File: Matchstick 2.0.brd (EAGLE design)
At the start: 73 x 38 mm, 13 parts, among them IC1 74HCT125D, J1 694106301002, J2 TARGET, J3 691241510006, J4 691241510006, U1 M5STAMP PICO

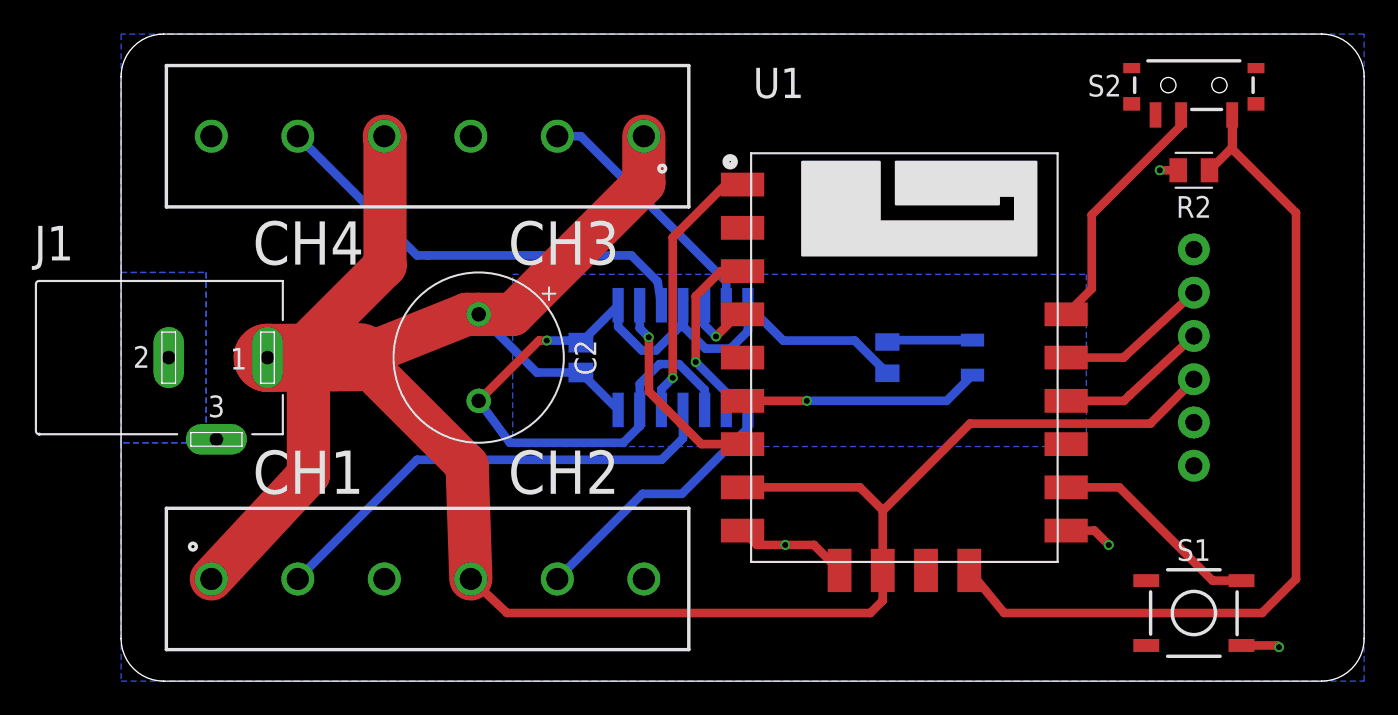
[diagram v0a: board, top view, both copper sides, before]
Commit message: adjusting traces for solderability
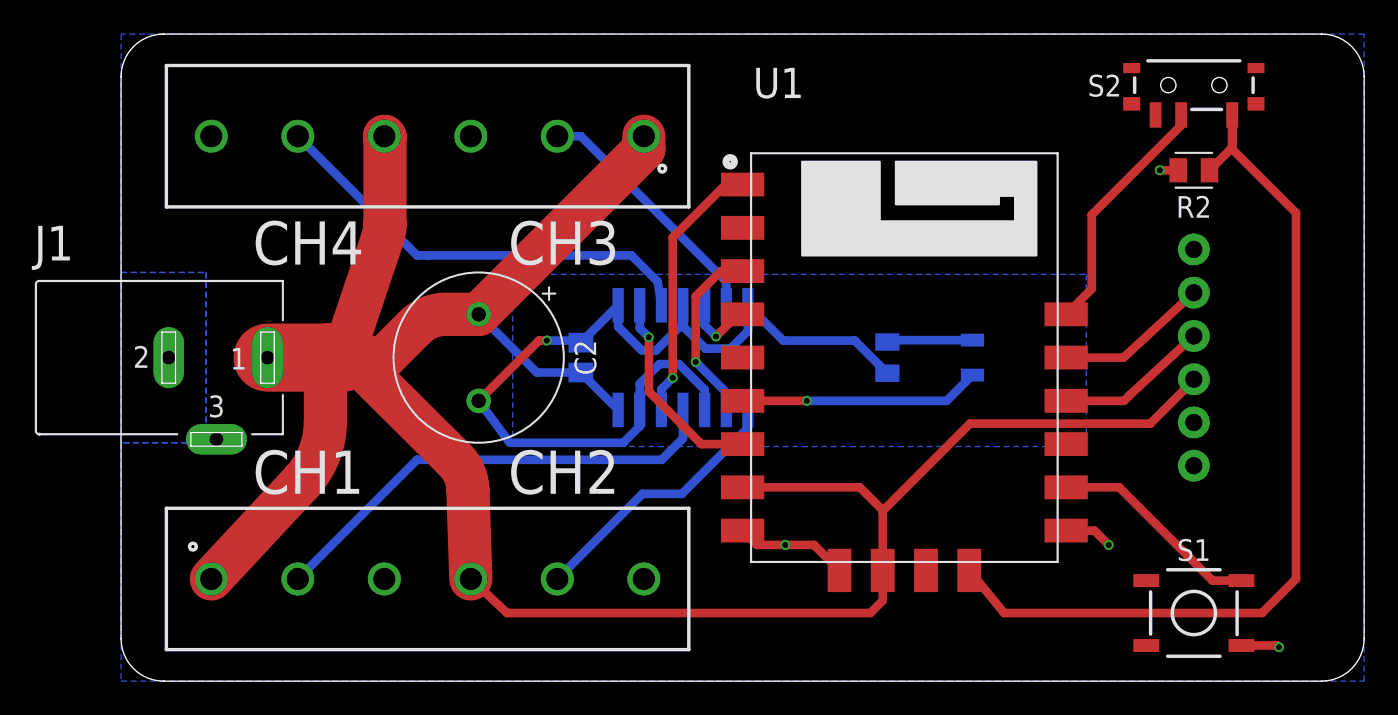
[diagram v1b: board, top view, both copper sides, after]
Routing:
- net VCC: track 155.1 -> 145.6 mm
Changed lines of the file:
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@@
 <wire x1="63" y1="17.73" x2="62.98" y2="17.65605" width="0.508" layer="1"/>
 <wire x1="62.98" y1="17.65605" x2="60.44755" y2="15.1236" width="0.508" layer="1"/>
-<wire x1="20.54" y1="6" x2="20.32" y2="12.68" width="2.54" layer="1"/>
+<wire x1="20.54" y1="6" x2="20.36624375" y2="11.2758625" width="2.54" layer="1"/>
+<wire x1="20.36624375" y1="11.2758625" x2="19.6312375" y2="12.96549375" width="2.54" layer="1" curve="43.247949"/>
+<wire x1="19.6312375" y1="12.96549375" x2="13.56851875" y2="19" width="2.54" layer="1"/>
 <wire x1="20.54" y1="6" x2="22.67" y2="4" width="0.508" layer="1"/>
 <wire x1="15.46" y1="32" x2="15.5" y2="31.96" width="2.54" layer="1"/>
-<wire x1="15.5" y1="31.96" x2="15.5" y2="24.4" width="2.54" layer="1"/>
-<wire x1="5.3" y1="6" x2="11" y2="12.121946875" width="2.54" layer="1"/>
-<wire x1="15.5" y1="24.4" x2="10.13125" y2="19.03125" width="2.54" layer="1"/>
-<wire x1="10.13125" y1="19.03125" x2="8.6" y2="19" width="2.54" layer="1"/>
-<wire x1="8.6" y1="19" x2="8.62166875" y2="18.97833125" width="4" layer="1"/>
-<wire x1="14" y1="19.02418125" x2="8.62166875" y2="18.97833125" width="4" layer="1"/>
-<wire x1="20.293171875" y1="21.54" x2="14" y2="19.02418125" width="2.54" layer="1"/>
-<wire x1="20.293171875" y1="21.54" x2="21" y2="21.54" width="2.54" layer="1"/>
-<wire x1="11" y1="12.121946875" x2="11" y2="18.57681875" width="2.54" layer="1"/>
-<wire x1="8.6" y1="19" x2="10.579684375" y2="19" width="2.54" layer="1"/>
-<wire x1="11" y1="18.57681875" x2="10.579684375" y2="19" width="2.54" layer="1"/>
-<wire x1="20.32" y1="12.68" x2="13.95" y2="19.05" width="2.54" layer="1"/>
-<wire x1="13.95" y1="19.05" x2="8.6" y2="19" width="2.54" layer="1"/>
+<wire x1="15.5" y1="31.96" x2="15.5" y2="26.84138125" width="2.54" layer="1"/>
+<wire x1="15.5" y1="26.84138125" x2="15.3695375" y2="26.04433125" width="2.54" layer="1" curve="-18.591584"/>
+<wire x1="15.3695375" y1="26.04433125" x2="13" y2="19" width="2.54" layer="1"/>
+<wire x1="5.3" y1="6" x2="10.59781875" y2="11.68999375" width="2.54" layer="1"/>
+<wire x1="10.59781875" y1="11.68999375" x2="12" y2="15.2536625" width="2.54" layer="1" curve="42.955877"/>
+<wire x1="12" y1="15.2536625" x2="12" y2="19" width="2.54" layer="1"/>
 <wire x1="44.73" y1="4.73" x2="44.73" y2="6.5" width="0.508" layer="1"/>
 <wire x1="44" y1="4" x2="44.73" y2="4.73" width="0.508" layer="1"/>
@@
 <wire x1="44.73" y1="10" x2="44.73" y2="6.5" width="0.508" layer="1"/>
 <wire x1="43.382" y1="11.38" x2="44.73" y2="10.032" width="0.508" layer="1"/>
-<wire x1="21" y1="21.54" x2="23" y2="21.54" width="2.54" layer="1"/>
-<wire x1="30.7" y1="29.24" x2="23" y2="21.54" width="2.54" layer="1"/>
-<wire x1="30.7" y1="29.24" x2="30.7" y2="32" width="2.54" layer="1"/>
+<wire x1="30.7" y1="31.24" x2="21" y2="21.54" width="2.54" layer="1"/>
+<wire x1="30.7" y1="31.24" x2="30.7" y2="32" width="2.54" layer="1"/>
 <wire x1="21" y1="21.54" x2="24.4154" y2="18.1246" width="0.508" layer="16"/>
 <wire x1="24.4154" y1="18.1246" x2="27" y2="18.1246" width="0.508" layer="16"/>
@@
 <wire x1="49.8536" y1="15.1236" x2="44.73" y2="10" width="0.508" layer="1"/>
 <wire x1="60.44755" y1="15.1236" x2="49.8536" y2="15.1236" width="0.508" layer="1"/>
+<wire x1="21" y1="21.54" x2="19.035534375" y2="21.54" width="2.54" layer="1"/>
+<wire x1="19.035534375" y1="21.54" x2="17.267765625" y2="20.807765625" width="2.54" layer="1" curve="45.000051"/>
+<wire x1="17.267765625" y1="20.807765625" x2="15.46" y2="19" width="2.54" layer="1"/>
+<wire x1="15.46" y1="19" x2="13.56851875" y2="19" width="2.54" layer="1"/>
+<wire x1="13.56851875" y1="19" x2="13" y2="19" width="2.54" layer="1"/>
+<wire x1="13" y1="19" x2="12" y2="19" width="2.54" layer="1"/>
+<wire x1="12" y1="19" x2="13" y2="19" width="4" layer="1"/>
+<wire x1="13" y1="19" x2="8.6" y2="19" width="4" layer="1"/>
 </signal>
 <signal name="G0">

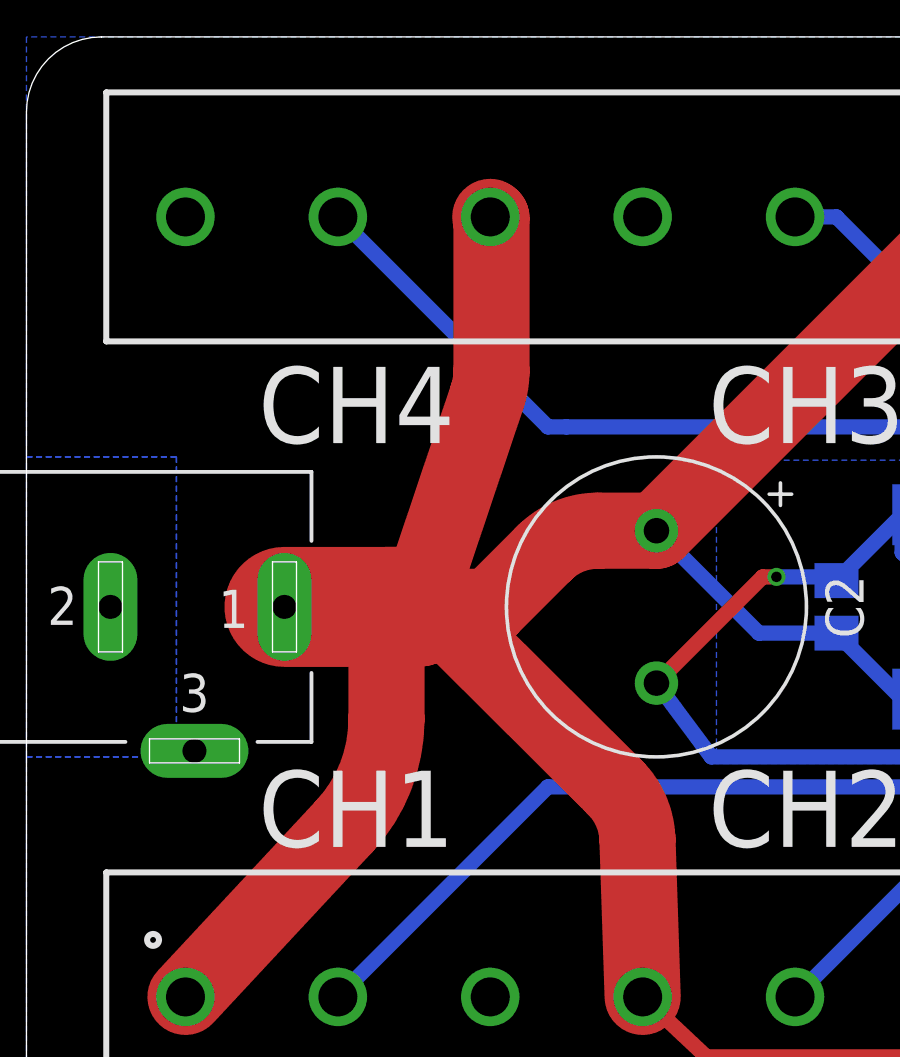
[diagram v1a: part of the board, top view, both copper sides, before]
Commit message: adjusting traces for solderability
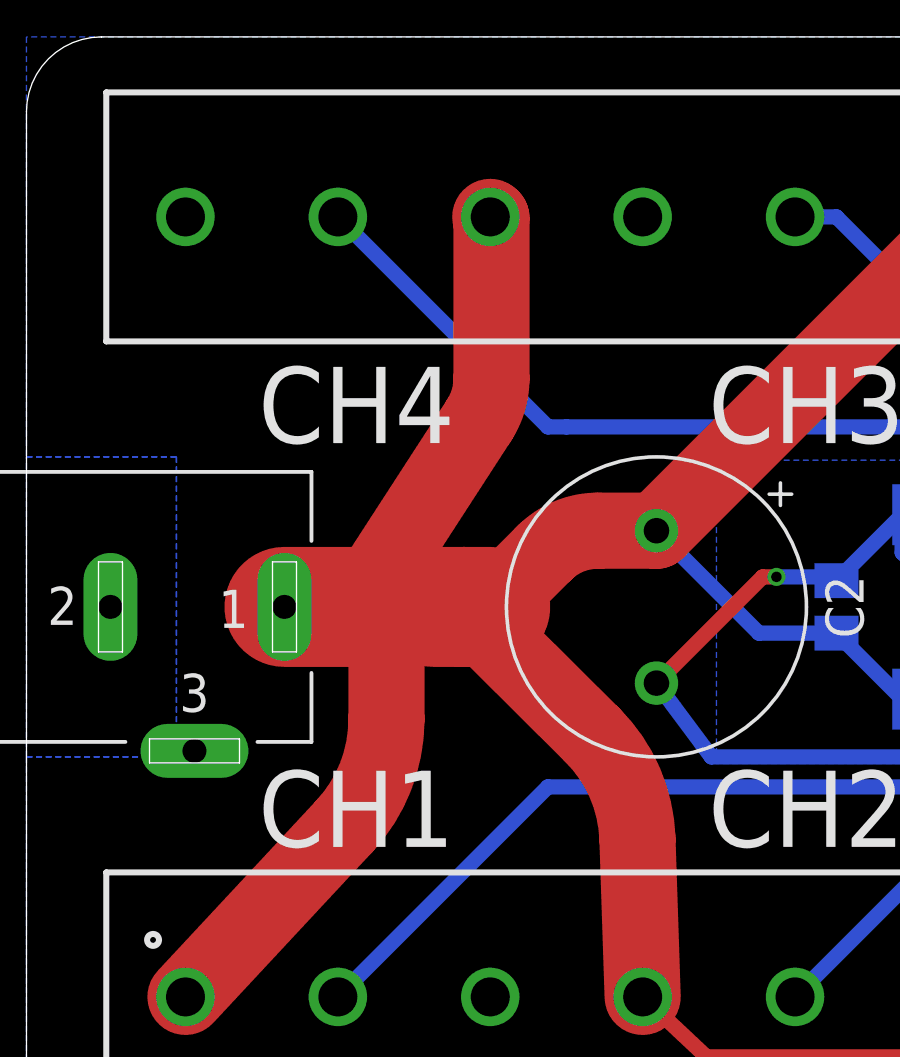
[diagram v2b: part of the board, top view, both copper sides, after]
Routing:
- net VCC: track 145.6 -> 143.9 mm
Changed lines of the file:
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@@
 <wire x1="62.98" y1="17.65605" x2="60.44755" y2="15.1236" width="0.508" layer="1"/>
 <wire x1="20.54" y1="6" x2="20.36624375" y2="11.2758625" width="2.54" layer="1"/>
-<wire x1="20.36624375" y1="11.2758625" x2="19.6312375" y2="12.96549375" width="2.54" layer="1" curve="43.247949"/>
-<wire x1="19.6312375" y1="12.96549375" x2="13.56851875" y2="19" width="2.54" layer="1"/>
+<wire x1="20.36624375" y1="11.2758625" x2="18.8676125" y2="14.720909375" width="2.54" layer="1" curve="43.247949"/>
+<wire x1="18.8676125" y1="14.720909375" x2="14.56851875" y2="19" width="2.54" layer="1"/>
 <wire x1="20.54" y1="6" x2="22.67" y2="4" width="0.508" layer="1"/>
 <wire x1="15.46" y1="32" x2="15.5" y2="31.96" width="2.54" layer="1"/>
-<wire x1="15.5" y1="31.96" x2="15.5" y2="26.84138125" width="2.54" layer="1"/>
-<wire x1="15.5" y1="26.84138125" x2="15.3695375" y2="26.04433125" width="2.54" layer="1" curve="-18.591584"/>
-<wire x1="15.3695375" y1="26.04433125" x2="13" y2="19" width="2.54" layer="1"/>
+<wire x1="15.5" y1="31.96" x2="15.5" y2="26.596471875" width="2.54" layer="1"/>
+<wire x1="15.5" y1="26.596471875" x2="15.09788125" y2="25.23673125" width="2.54" layer="1" curve="-32.949269"/>
+<wire x1="15.09788125" y1="25.23673125" x2="11.05555625" y2="19" width="2.54" layer="1"/>
 <wire x1="5.3" y1="6" x2="10.59781875" y2="11.68999375" width="2.54" layer="1"/>
 <wire x1="10.59781875" y1="11.68999375" x2="12" y2="15.2536625" width="2.54" layer="1" curve="42.955877"/>
@@
 <wire x1="19.035534375" y1="21.54" x2="17.267765625" y2="20.807765625" width="2.54" layer="1" curve="45.000051"/>
 <wire x1="17.267765625" y1="20.807765625" x2="15.46" y2="19" width="2.54" layer="1"/>
-<wire x1="15.46" y1="19" x2="13.56851875" y2="19" width="2.54" layer="1"/>
-<wire x1="13.56851875" y1="19" x2="13" y2="19" width="2.54" layer="1"/>
-<wire x1="13" y1="19" x2="12" y2="19" width="2.54" layer="1"/>
-<wire x1="12" y1="19" x2="13" y2="19" width="4" layer="1"/>
-<wire x1="13" y1="19" x2="8.6" y2="19" width="4" layer="1"/>
+<wire x1="15.46" y1="19" x2="14.56851875" y2="19" width="4" layer="1"/>
+<wire x1="14.56851875" y1="19" x2="13.56851875" y2="19" width="4" layer="1"/>
+<wire x1="13.56851875" y1="19" x2="12" y2="19" width="2.54" layer="1"/>
+<wire x1="12" y1="19" x2="11.05555625" y2="19" width="4" layer="1"/>
+<wire x1="11.05555625" y1="19" x2="8.6" y2="19" width="4" layer="1"/>
 </signal>
 <signal name="G0">
